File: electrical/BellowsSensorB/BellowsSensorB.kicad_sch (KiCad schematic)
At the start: 5 parts, among them J1 I2C, U1 WF200DPZ 0.1BG S16 DT

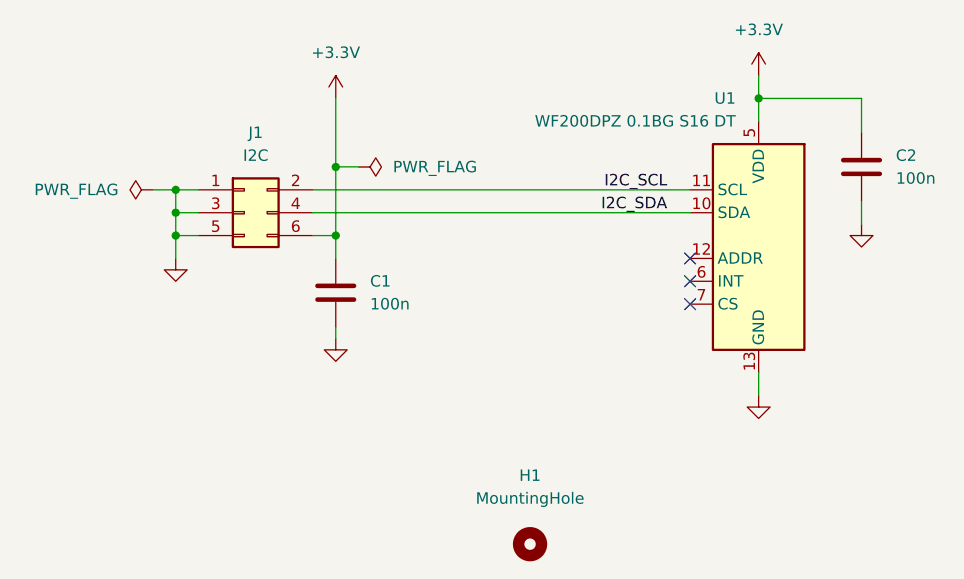
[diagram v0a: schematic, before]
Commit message: Add solder bridges to BellowsSensorB
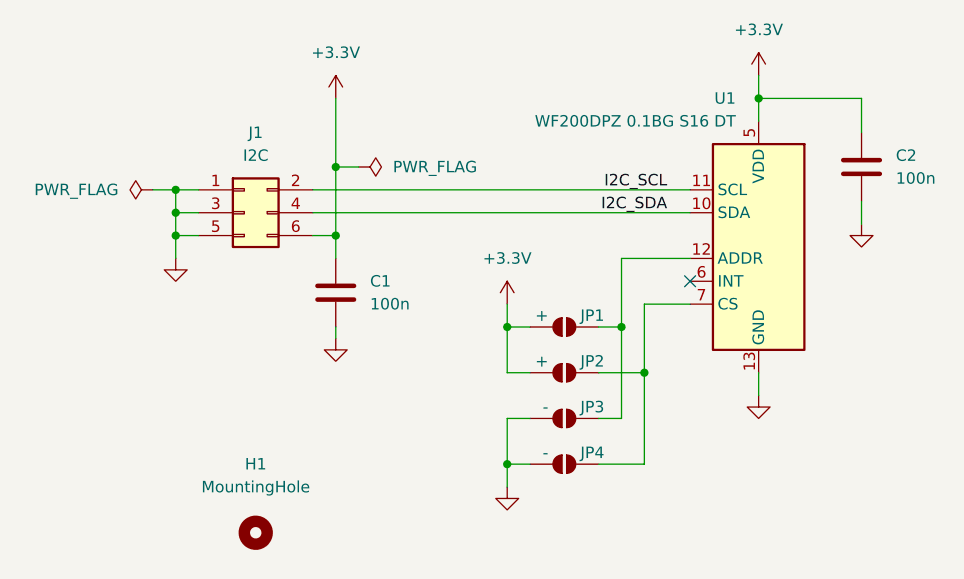
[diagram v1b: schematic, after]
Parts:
- added JP1, JP2: +, Jumper:SolderJumper-2_P1.3mm_Open_RoundedPad1.0x1.5mm, symbol Jumper:SolderJumper_2_Open
- added JP3, JP4: -, Jumper:SolderJumper-2_P1.3mm_Open_RoundedPad1.0x1.5mm, symbol Jumper:SolderJumper_2_Open
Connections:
- net +3.3V: now also JP1.2 (B), JP2.2 (B)
- net GND: now also JP3.2 (B), JP4.2 (B)
- net at U1.12 (ADDR): now also JP1.1 (A), JP3.1 (A)
- net at U1.7 (CS): now also JP2.1 (A), JP4.1 (A)
- no-connect marks 3 -> 1
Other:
- moved on the sheet: H1
